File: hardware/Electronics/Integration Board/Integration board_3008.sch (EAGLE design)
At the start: 11 parts, among them J3 CONN_20X2

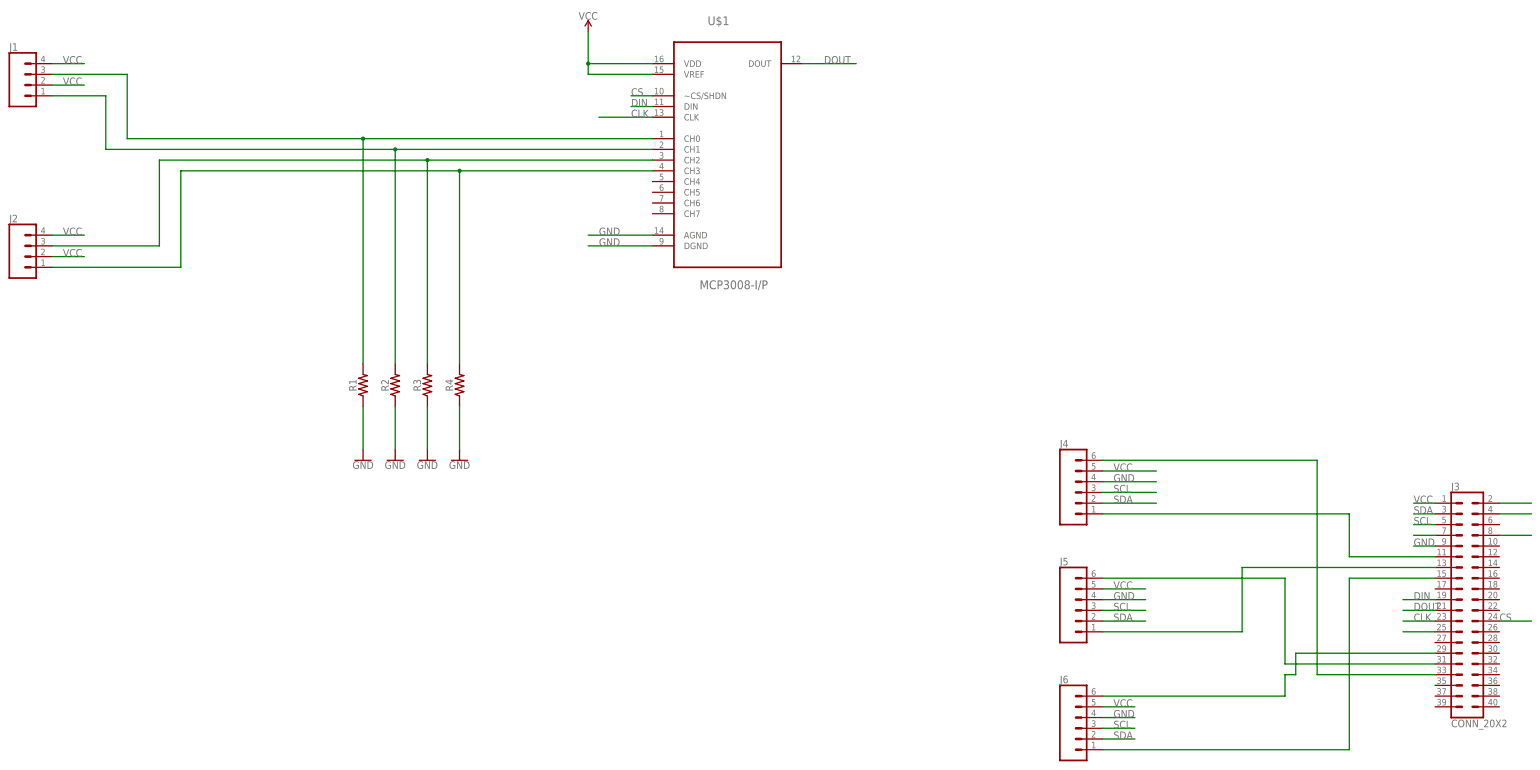
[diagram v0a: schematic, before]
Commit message: Added IMU and Integration board schematic and layout PNG's
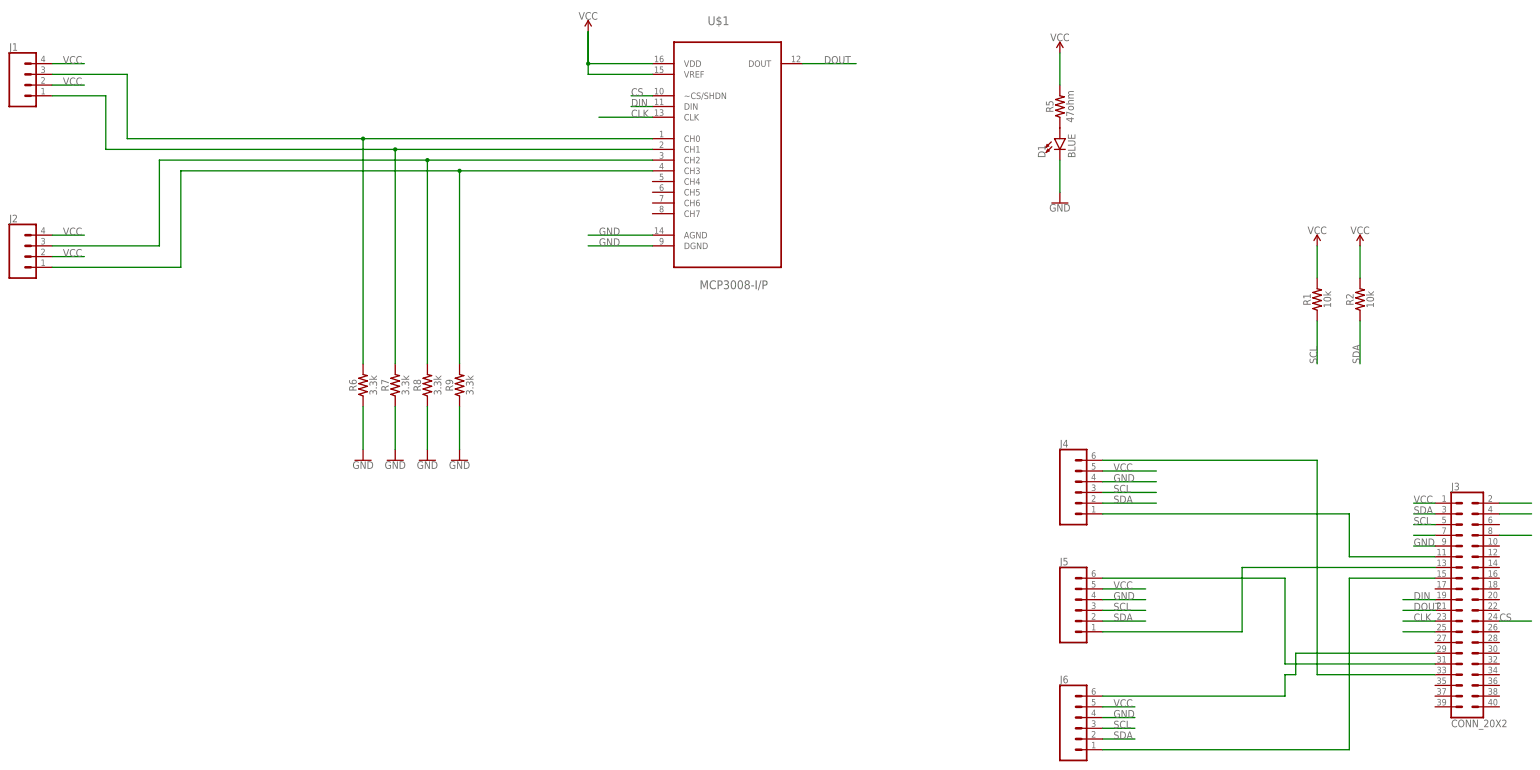
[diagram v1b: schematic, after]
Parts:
- removed R3, R4: (no value), SparkFun-Resistors:RESISTORAXIAL-0.3
- added D1: BLUE, SparkFun-LED:LED-BLUE0603
- added R5: 47ohm, SparkFun-Resistors:RESISTOR0805
- added R6, R7, R8, R9: 3.3k, SparkFun-Resistors:RESISTOR0805
- R1, R2: value (none) -> 10k; device SparkFun-Resistors:RESISTORAXIAL-0.3 -> SparkFun-Resistors:RESISTOR0805
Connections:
- new net N$11: D1.A, R5.1
- net GND: now also D1.C, R6.1, R7.1, R8.1, R9.1; no longer R1.1, R2.1, R3.1, R4.1
- net N$1: now also R6.2; no longer R1.2
- net N$15: now also R7.2; no longer R2.2
- net N$3: now also R8.2; no longer R3.2
- net N$4: now also R9.2; no longer R4.2
- net SCL: now also R1.1
- net SDA: now also R2.1
- net VCC: now also R1.2, R2.2, R5.2
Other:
- moved on the sheet: R1, R2
